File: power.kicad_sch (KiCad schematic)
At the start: 41 parts, among them J2 BATT_CON, J3 PWR_HDR, J4 NCT_BYPASS, U2 BQ25622, U6 MIC2876-5.25YMT-TR

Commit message: fix: modifications after driver completion
- Added missing RTC IRQ to PI
- RTC VBAT is not connected to the Main Battery trough a ~1k resistor
- Connected BQ CE through a Push-pull to Open-Drain converter to PI
- Changed Mosfets to TI PicoStar model
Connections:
- net BAT renamed VBAT
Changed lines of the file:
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@@
+	)
+	(junction
+		(at 48.26 114.3)
+		(diameter 0)
+		(color 0 0 0 0)
 	)
 	(junction
@@
 	(wire
 		(pts
+			(xy 44.45 114.3) (xy 48.26 114.3)
+		)
+		(stroke
+			(width 0)
+			(type default)
+		)
+	)
+	(wire
+		(pts
 			(xy 36.83 180.34) (xy 36.83 182.88)
 		)
@@
 	(wire
 		(pts
-			(xy 48.26 119.38) (xy 48.26 121.92)
+			(xy 48.26 110.49) (xy 48.26 114.3)
 		)
 		(stroke
@@
 		(pts
 			(xy 167.64 67.31) (xy 196.85 67.31)
+		)
+		(stroke
+			(width 0)
+			(type default)
+		)
+	)
+	(wire
+		(pts
+			(xy 48.26 114.3) (xy 48.26 121.92)
 		)
 		(stroke
@@
 	)
 	(label "BAT"
-		(at 48.26 119.38 0)
+		(at 48.26 110.49 0)
 		(fields_autoplaced yes)
 		(effects
@@
 		(fields_autoplaced yes)
 		(effects
+			(font
+				(size 1.27 1.27)
+			)
+			(justify right)
+		)
+	)
+	(hierarchical_label "VBAT"
+		(shape output)
+		(at 44.45 114.3 180)
+		(fields_autoplaced yes)
+		(effects

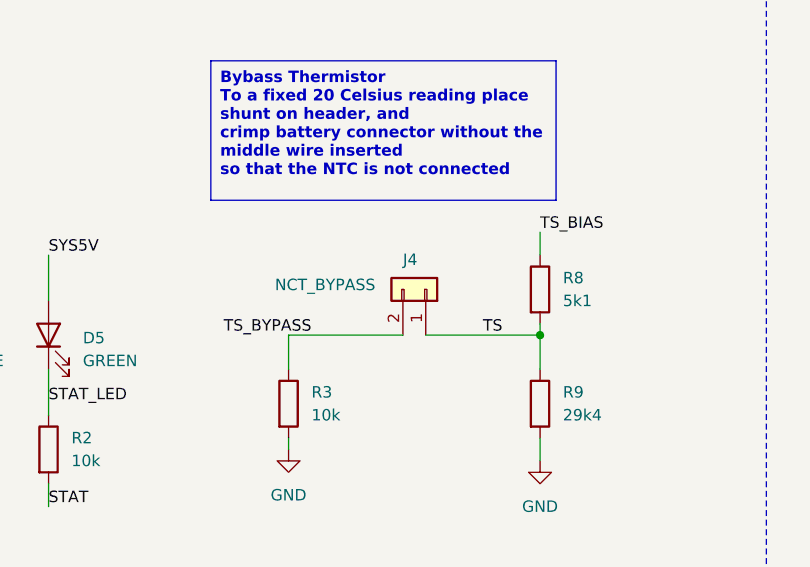
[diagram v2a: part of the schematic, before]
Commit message: fix: pcb changes, moved i2c ext header to 2x2 pin at the edge, pinout adjustments, silkscreen fixes
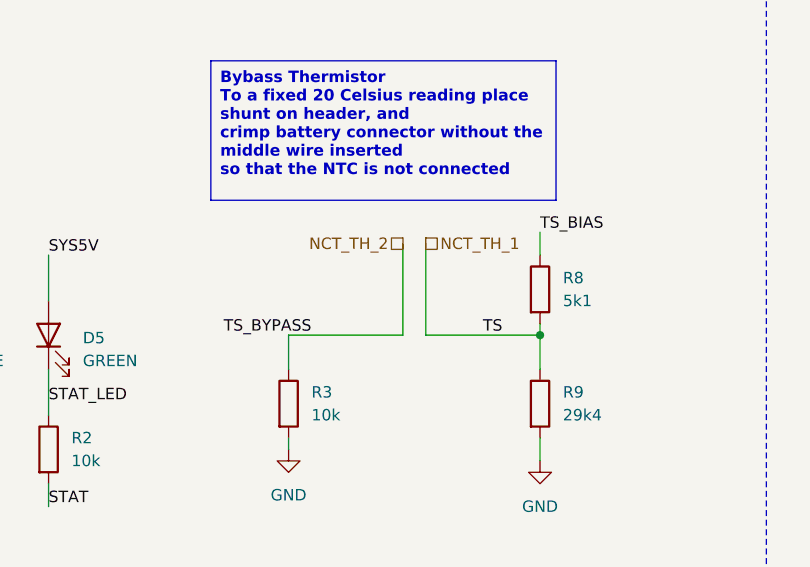
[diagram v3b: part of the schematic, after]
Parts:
- removed J4: NCT_BYPASS, Connector_PinHeader_2.54mm:PinHeader_1x02_P2.54mm_Vertical, symbol Connector_Generic:Conn_01x02
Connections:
- net TS renamed NCT_TH_1
- net TS_BYPASS renamed NCT_TH_2
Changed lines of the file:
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@@
+	(wire
+		(pts
+			(xy 118.11 160.02) (xy 118.11 170.18)
+		)
+		(stroke
+			(width 0)
+			(type default)
+		)
+	)
 	(wire
 		(pts
@@
 		(pts
 			(xy 105.41 170.18) (xy 118.11 170.18)
+		)
+		(stroke
+			(width 0)
+			(type default)
+		)
+	)
+	(wire
+		(pts
+			(xy 120.65 160.02) (xy 120.65 170.18)
 		)
 		(stroke
@@
 		)
 	)
+	(hierarchical_label "NCT_TH_2"
+		(shape passive)
+		(at 118.11 160.02 180)
+		(fields_autoplaced yes)
+		(effects
+			(font
+				(size 1.27 1.27)
+			)
+			(justify right)
+		)
+	)
 	(hierarchical_label "VBUS_F"
 		(shape output)
 		(at 118.11 22.86 0)
+		(fields_autoplaced yes)
+		(effects
+			(font
+				(size 1.27 1.27)
+			)
+			(justify left)
+		)
+	)
+	(hierarchical_label "NCT_TH_1"
+		(shape passive)
+		(at 120.65 160.02 0)
 		(fields_autoplaced yes)
 		(effects
@@
 					(unit 1)
 				)
-			)
-		)
-	)
-	(symbol
-		(lib_id "Connector_Generic:Conn_01x02")
-		(at 120.65 165.1 270)
-		(mirror x)
-		(unit 1)
-		(exclude_from_sim no)
-		(in_bom yes)
-		(on_board yes)
-		(dnp no)
-		(property "Reference" "J4"
-			(at 118.11 161.798 90)
-			(effects
-				(font
-					(size 1.27 1.27)
-				)
-				(justify left)
-			)
-		)
-		(property "Value" "NCT_BYPASS"
-			(at 103.886 164.592 90)
-			(effects
-				(font
-					(size 1.27 1.27)
-				)
-				(justify left)
-			)
-		)
-		(property "Footprint" "Connector_PinHeader_2.54mm:PinHeader_1x02_P2.54mm_Vertical"
-			(at 120.65 165.1 0)
-			(effects
-				(font
-					(size 1.27 1.27)
-				)
-				(hide yes)
-			)
-		)
-		(property "Datasheet" "~"
-			(at 120.65 165.1 0)
-			(effects
-				(font
-					(size 1.27 1.27)
-				)
-				(hide yes)
-			)
-		)
-		(property "Description" "Generic connector, single row, 01x02, script generated (kicad-library-utils/schlib/autogen/connector/)"
-			(at 120.65 165.1 0)
-			(effects
-				(font
-					(size 1.27 1.27)
-				)
-				(hide yes)
-			)
-		)
-		(property "MPN" "61300211121"
-			(at 120.65 165.1 0)
-			(effects
-				(font
-					(size 1.27 1.27)
-				)
-				(hide yes)
-			)
-		)
-		(property "Manufacturer" "Würth Elektronik"
-			(at 120.65 165.1 0)
-			(effects
-				(font
-					(size 1.27 1.27)
-				)
-				(hide yes)
-			)
-		)
-		(pin "2"
-		)
-		(pin "1"
-		)
-		(instances
-			(project "effectiveRangeHat_simple"
-				(path "/6edc5e63-ec2a-49cc-8eeb-48e0d5e90dc6/d94d9111-a93b-4c7b-9c75-80efdb5e75c6"
-					(reference "J4")
-					(unit 1)
-				)
